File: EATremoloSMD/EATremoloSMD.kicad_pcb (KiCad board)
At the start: 2 copper layers, 31 x 85.1 mm, 38 parts, among them J1 JACK__MONO_2P_NC, J2 BARREL_JACK, J3 JACK__MONO_2P_NC, Q1 Q_NJFET_DSG, Q2 Q_NPN_EBC, Q3 Q_NPN_EBC, Q4 Q_NJFET_DSG, SW1 SW_3PDT_on_on

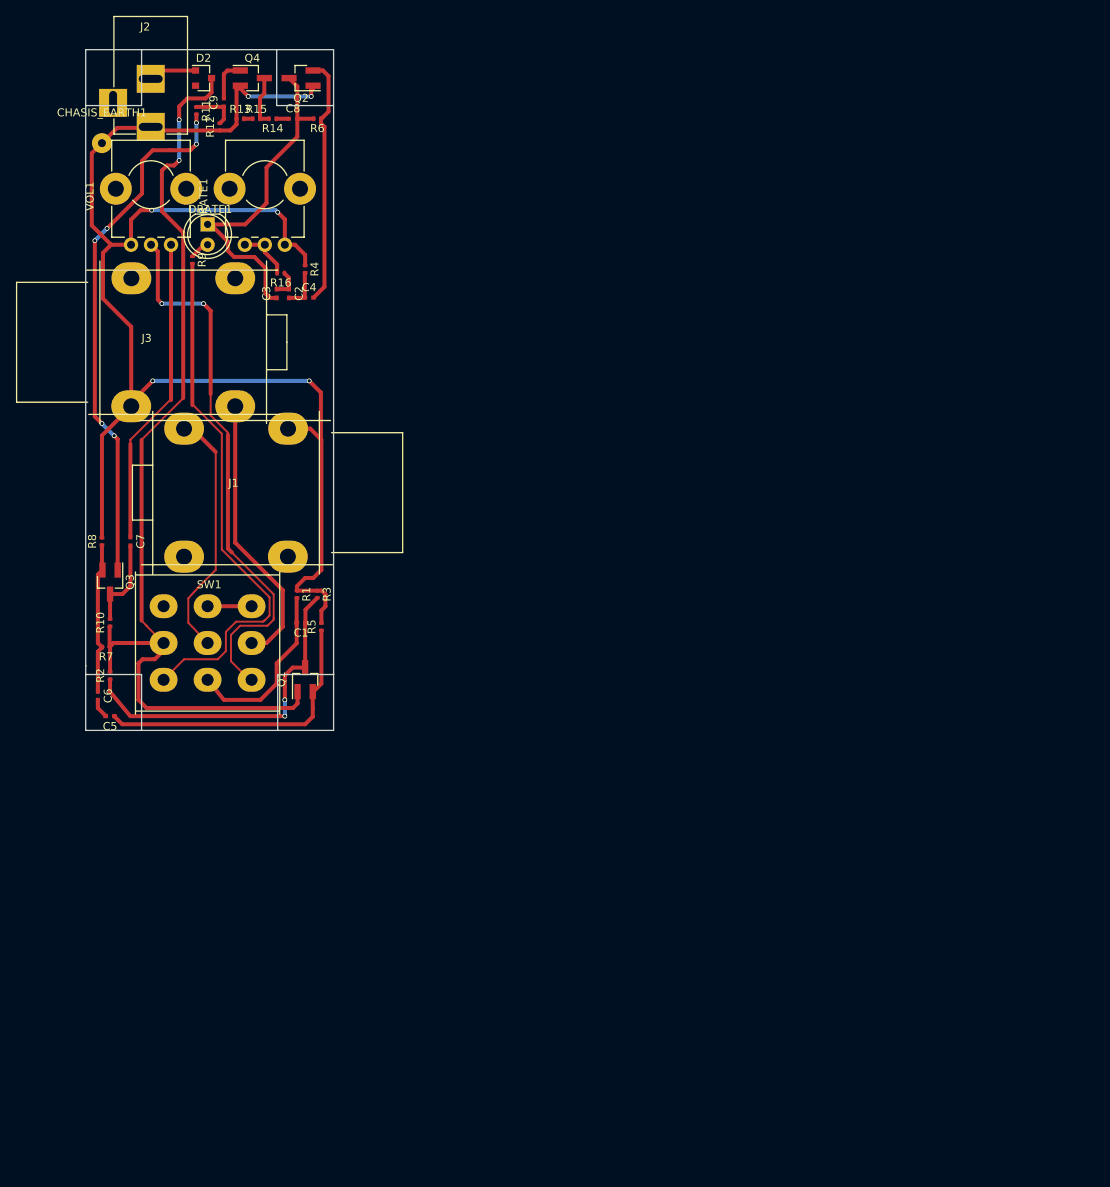
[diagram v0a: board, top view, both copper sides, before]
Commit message: Updated EATremoloSMD
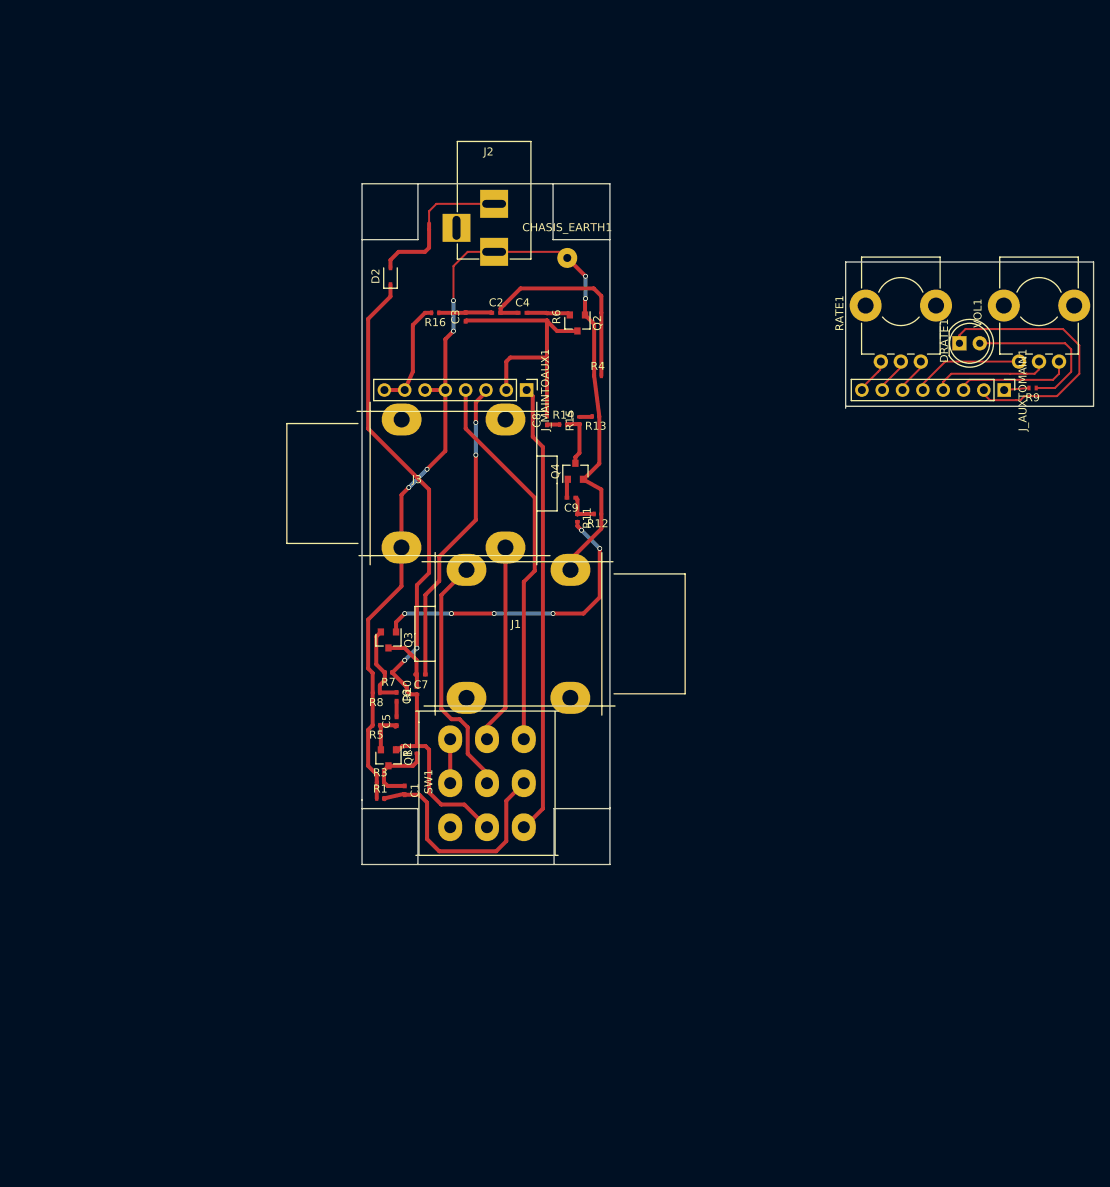
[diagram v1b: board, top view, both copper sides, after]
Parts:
- added J_AUXTOMAIN1: CONN_01X08, Pin_Headers:Pin_Header_Straight_1x08_Pitch2.54mm, F.Cu at (182.1, 86.9)
- added J_MAINTOAUX1: CONN_01X08, Pin_Headers:Pin_Header_Straight_1x08_Pitch2.54mm, F.Cu at (122.4, 86.9)
- D2: footprint Diodes_SMD:D_SOT-23_ANK -> Diodes_SMD:D_SOD-323
- Q1, Q2, Q3, Q4: footprint TO_SOT_Packages_SMD:SOT-23_Handsoldering -> TO_SOT_Packages_SMD:SOT-23
- moved VOL1 112.0 mm to (189.0, 83.3)
- moved R9 106.2 mm to (185.7, 86.6), turned to 180 degrees
- moved DRATE1 95.1 mm to (176.5, 81.0), turned to 0 degrees
- moved RATE1 80.8 mm to (171.7, 83.3)
- moved R11 69.7 mm to (128.8, 102.9)
- moved R12 67.6 mm to (131.3, 102.4), turned to 180 degrees
- moved C9 65.8 mm to (128.0, 100.3), turned to 180 degrees
- moved Q4 63.6 mm to (128.5, 97.0), turned to 90 degrees
- moved CHASIS_EARTH1 59.9 mm to (127.5, 70.4)
- moved R13 58.0 mm to (131.1, 90.2), turned to 180 degrees
- moved R15 55.3 mm to (129.0, 90.7), turned to 90 degrees
- moved R14 52.7 mm to (127.0, 91.2), turned to 0 degrees
- moved C8 49.3 mm to (125.0, 90.7), turned to 90 degrees
- moved Q2 46.2 mm to (128.8, 78.5), turned to 270 degrees
- moved J2 45.7 mm to (118.4, 69.6)
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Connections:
- C3 pad 1: Net-(C3-Pad1) -> /LED_AN
- C7 pad 1: Net-(C7-Pad1) -> /VOL_P3
- C8 pad 2: Net-(C3-Pad1) -> /LED_AN
- DRATE1 pad 1: Net-(C3-Pad1) -> Net-(DRATE1-Pad1)
- Q2 pad 3: Net-(C3-Pad1) -> /LED_AN
- R15 pad 1: Net-(R13-Pad2) -> Net-(Q4-Pad3)
- R15 pad 2: Net-(Q4-Pad3) -> Net-(R13-Pad2)
- R16 pad 2: Net-(R16-Pad2) -> /RATE_P1
- R6 pad 2: Net-(C3-Pad1) -> /LED_AN
- R9 pad 2: Net-(R9-Pad2) -> Net-(J_AUXTOMAIN1-Pad1)
- RATE1 pad 1: /GND -> Net-(J_AUXTOMAIN1-Pad6)
- RATE1 pad 2: Net-(R16-Pad2) -> Net-(J_AUXTOMAIN1-Pad7)
- RATE1 pad 3: Net-(R16-Pad2) -> Net-(J_AUXTOMAIN1-Pad8)
- SW1 pad 3: Net-(R9-Pad2) -> /LED_CA
- SW1 pad 9: Net-(SW1-Pad9) -> /VOL_P2
- VOL1 pad 1: Net-(C7-Pad1) -> Net-(J_AUXTOMAIN1-Pad3)
- VOL1 pad 2: Net-(SW1-Pad9) -> Net-(J_AUXTOMAIN1-Pad4)
- VOL1 pad 3: /GND -> Net-(J_AUXTOMAIN1-Pad5)
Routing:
- net Net-(SW1-Pad9): track 69.4 -> 0.00 mm, vias 2 -> 0
- net Net-(R9-Pad2): track 66.1 -> 0.00 mm
- net /LED_CA: track 0.00 -> 56.5 mm
- net /GND: track 186.7 -> 134.0 mm
- net /VOL_P2: track 0.00 -> 47.8 mm
- net Net-(C3-Pad1): track 43.1 -> 0.00 mm
- net /+9V: track 123.6 -> 84.8 mm
- net Net-(C7-Pad1): track 38.7 -> 0.00 mm
- net /VOL_P3: track 0.00 -> 38.7 mm, vias 0 -> 2
- net /LED_AN: track 0.00 -> 35.4 mm
- net Net-(DRATE1-Pad1): track 0.00 -> 34.8 mm
- net Net-(C1-Pad1): track 42.2 -> 9.93 mm, vias 2 -> 0
- net Net-(C5-Pad1): track 36.9 -> 5.46 mm
- net Net-(Q3-Pad1): track 66.2 -> 38.6 mm
- net Net-(C4-Pad2): track 31.1 -> 5.47 mm
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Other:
- board size 31 x 85.1 mm -> 91.4 x 85.1 mm

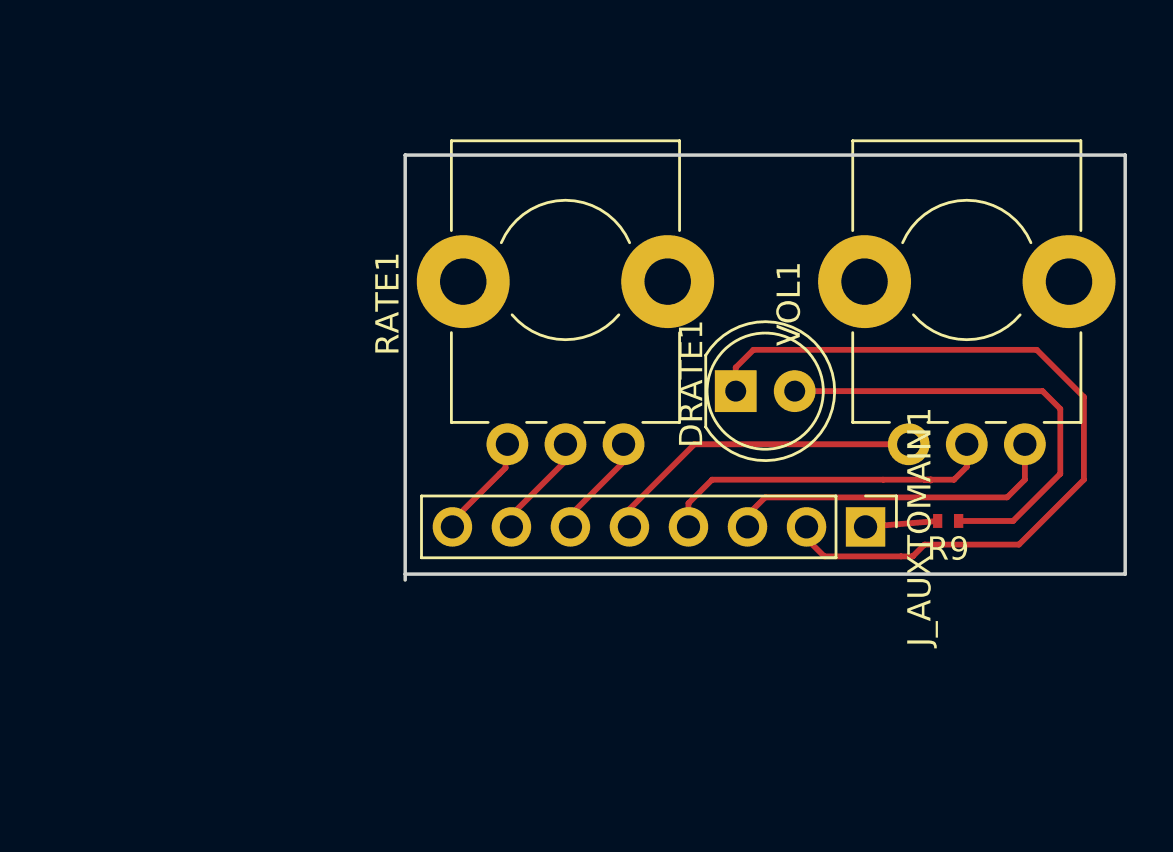
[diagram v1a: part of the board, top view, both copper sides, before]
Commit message: EAMTremoloSMD update
pcb header alignment
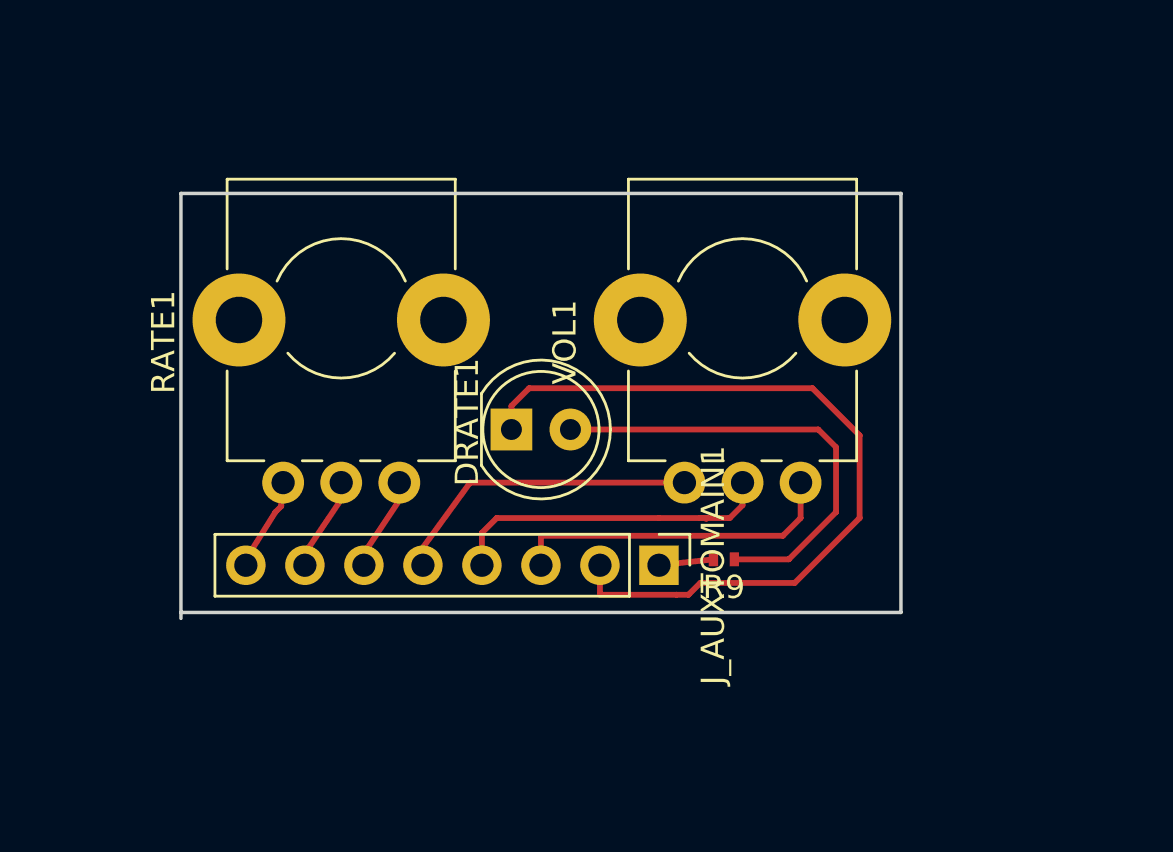
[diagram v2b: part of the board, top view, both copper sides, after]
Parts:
- moved DRATE1 9.79 mm to (166.9, 82.7)
- moved R9 9.79 mm to (176.0, 88.3)
- moved RATE1 9.79 mm to (162.1, 85.0)
- moved VOL1 9.79 mm to (179.3, 85.0)
- moved J_AUXTOMAIN1 9.04 mm to (173.2, 88.5)
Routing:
- net Net-(J_AUXTOMAIN1-Pad1): track 3.12 -> 2.36 mm
- net Net-(J_AUXTOMAIN1-Pad4): track 15.0 -> 14.5 mm
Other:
- board size 91.4 x 85.1 mm -> 81.8 x 85.1 mm

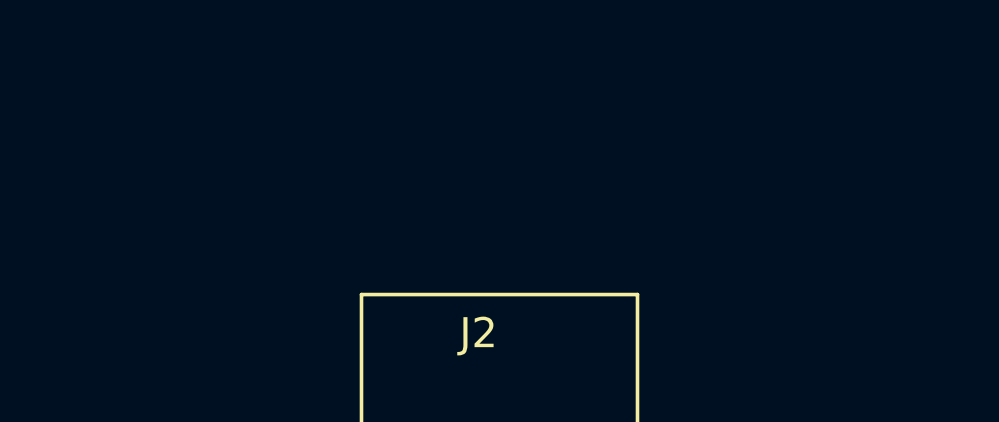
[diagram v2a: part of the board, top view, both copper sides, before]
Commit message: Board Description Updates
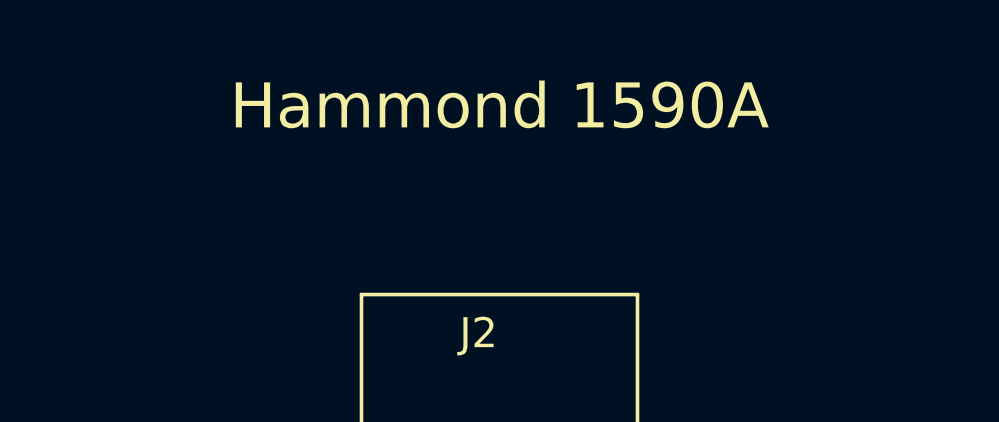
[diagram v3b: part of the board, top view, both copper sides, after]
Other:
- board text added: "Hammond 1590A"
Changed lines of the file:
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@@
     (links 68)
     (no_connects 0)
-    (area 92.180999 55.370999 195.201 146.252001)
+    (area 92.180999 48.33 185.549 146.252001)
     (thickness 1.6)
-    (drawings 18)
+    (drawings 19)
     (tracks 270)
     (zones 0)
@@
       (rotate (xyz 0 0 0))
     )
+  )
+  (gr_text "Hammond 1590A" (at 118.364 49.53) (layer F.SilkS)
+    (effects (font (size 1.5 1.5) (thickness 0.3)))
   )
   (gr_line (start 183.642 90.551) (end 152.654 90.551) (angle 90) (layer Edge.Cuts) (width 0.15))
@@
   (segment (start 123.444 109.474) (end 123.444 100.33) (width 0.5) (layer F.Cu) (net 36))
   (segment (start 122.075 110.843) (end 123.444 109.474) (width 0.5) (layer F.Cu) (net 36))
-  (segment (start 165.608 88.519) (end 165.608 87.122) (width 0.25) (layer F.Cu) (net 37) (status 400000))
+  (segment (start 165.608 88.519) (end 165.608 87.122) (width 0.25) (layer F.Cu) (net 37))
   (segment (start 165.608 87.122) (end 166.243 86.487) (width 0.25) (layer F.Cu) (net 37))
   (segment (start 173.228 86.487) (end 166.243 86.487) (width 0.25) (layer F.Cu) (net 37))

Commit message: updates
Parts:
- SW1: footprint custom_sw:SW_3PDT_W18MM_L17.3MM_P5.3MM_D2MM -> custom_sw:SW_3PDT_W18MM_L17.3MM_P5.3MM_D2MM_SolderLugs
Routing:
- net /LED_CA: track 56.5 -> 57.1 mm

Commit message: BoardUpdate
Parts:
- C1, C2, C3, C4, C5, C6, C7, C8, C9: footprint Capacitors_SMD:C_0402_NoSilk -> Capacitors_SMD:C_0805
- R1, R10, R11, R12, R13, R14, R15, R16, R2, R3, R4, R5, R6, R7, R8, R9: footprint Resistors_SMD:R_0402_NoSilk -> Resistors_SMD:R_0805
- moved J_AUXTOMAIN1 114.1 mm to (108.0, 182.1)
- moved VOL1 113.5 mm to (114.0, 177.8)
- moved RATE1 113.5 mm to (96.8, 177.8)
- moved DRATE1 113.4 mm to (101.7, 175.5)
- moved R9 109.9 mm to (109.4, 175.6), turned to 0 degrees
- moved C8 26.5 mm to (98.5, 90.6), turned to 180 degrees
- moved R14 24.5 mm to (102.5, 90.4), turned to 270 degrees
- moved R13 23.6 mm to (107.4, 90.4), turned to 270 degrees
- moved R16 23.2 mm to (90.6, 88.2), turned to 270 degrees
- moved R6 20.1 mm to (106.9, 86.7)
- moved C2 20.1 mm to (99.3, 82.5)
- moved Q1 20.0 mm to (89.9, 145.9)
- moved Q2 19.7 mm to (110.9, 86.6)
- moved C4 19.5 mm to (103.5, 83.5), turned to 270 degrees
- moved R2 19.1 mm to (92.7, 142.2)
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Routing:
- net /GND: track 134.0 -> 171.1 mm, vias 6 -> 4
- net Net-(C1-Pad1): track 9.93 -> 44.2 mm
- net Net-(C6-Pad1): track 10.7 -> 38.3 mm
- net /VOL_P3: track 38.7 -> 17.0 mm
- net Net-(C1-Pad2): track 29.8 -> 10.6 mm
- net Net-(J_AUXTOMAIN1-Pad1): track 2.36 -> 18.7 mm
- net Net-(Q3-Pad1): track 38.6 -> 22.8 mm, vias 6 -> 2
- net Net-(DRATE1-Pad2): track 19.8 -> 4.34 mm
- net Net-(DRATE1-Pad1): track 34.5 -> 49.4 mm
- net Net-(C7-Pad2): track 7.75 -> 19.2 mm
- net Net-(C5-Pad1): track 5.46 -> 12.0 mm
- net /LED_AN: track 35.4 -> 29.0 mm
- net /VOL_P2: track 47.8 -> 54.0 mm
- net /+9V: track 84.8 -> 91.0 mm
- net Net-(Q4-Pad3): track 6.72 -> 12.8 mm
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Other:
- board size 81.8 x 85.1 mm -> 31.1 x 114.2 mm
- board text removed: "Hammond 1590A"

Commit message: Update
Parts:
- removed J_AUXTOMAIN1, J_MAINTOAUX1: CONN_01X08, Pin_Headers:Pin_Header_Straight_1x08_Pitch2.54mm
- added J_AUX2MAIN_1: CONN_01X04, Pin_Headers:Pin_Header_Straight_1x04_Pitch2.54mm, F.Cu at (125.7, 93.2)
- added J_AUX2MAIN_2: CONN_01X04, Pin_Headers:Pin_Header_Straight_1x04_Pitch2.54mm, F.Cu at (153.7, 93.2)
- added J_MAIN2AUX_1: CONN_01X04, Pin_Headers:Pin_Header_Straight_1x04_Pitch2.54mm, F.Cu at (89.2, 93.7)
- added J_MAIN2AUX_2: CONN_01X04, Pin_Headers:Pin_Header_Straight_1x04_Pitch2.54mm, F.Cu at (116.6, 93.3)
- C1, C2, C3, C4, C5, C6, C7, C8, C9, D2, Q1, Q2, Q3, Q4, R1, R10, R11, R12, R13, R14, R15, R2, R3, R4, R5, R6, R7, R8, R9: moved to B.Cu
- R16: value 1K -> 4K7; moved to B.Cu
- moved R9 98.3 mm to (145.4, 84.2), turned to 90 degrees
- moved RATE1 92.7 mm to (136.1, 93.9)
- moved VOL1 90.7 mm to (148.2, 93.9)
- moved DRATE1 90.3 mm to (139.7, 93.6), turned to 90 degrees
- moved R5 29.3 mm to (117.2, 141.1)
- moved R3 26.1 mm to (90.2, 140.1), turned to 270 degrees
- moved Q1 25.8 mm to (115.7, 145.5)
- moved C5 24.9 mm to (114.0, 130.3), turned to 180 degrees
- moved R11 23.8 mm to (89.8, 105.0)
- moved C1 22.9 mm to (90.2, 144.0), turned to 270 degrees
- moved Q4 21.0 mm to (94.5, 89.5), turned to 0 degrees
- moved R12 20.3 mm to (96.3, 107.1), turned to 90 degrees
- moved C9 16.1 mm to (96.3, 102.7)
- moved R13 13.7 mm to (94.5, 86.1), turned to 0 degrees
- moved R1 12.2 mm to (115.4, 126.9)
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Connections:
- C3 pad 1: /LED_AN -> /LED_CA
- C8 pad 2: /LED_AN -> /LED_CA
- Q2 pad 1: /GND -> Net-(C4-Pad2)
- Q2 pad 2: Net-(C4-Pad2) -> /GND
- Q2 pad 3: /LED_AN -> /LED_CA
- Q3 pad 1: Net-(Q3-Pad1) -> Net-(C6-Pad1)
- Q3 pad 2: Net-(C6-Pad1) -> Net-(Q3-Pad2)
- R11 pad 2: Net-(Q3-Pad1) -> Net-(Q3-Pad2)
- R6 pad 2: /LED_AN -> /LED_CA
- SW1 pad 3: /LED_CA -> /LED_AN
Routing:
- net Net-(C1-Pad2): track 10.6 -> 66.9 mm
- net /LED_AN: track 29.0 -> 78.4 mm, vias 0 -> 2
- net /LED_CA: track 62.7 -> 32.1 mm, vias 0 -> 4
- net Net-(DRATE1-Pad1): track 49.4 -> 20.4 mm
- net /+9V: track 91.0 -> 118.3 mm, vias 2 -> 4
- net Net-(Q3-Pad1): track 22.8 -> 0.00 mm, vias 2 -> 0
- net Net-(C5-Pad2): track 4.20 -> 23.2 mm, vias 0 -> 2
- net Net-(C7-Pad2): track 19.2 -> 35.6 mm, vias 0 -> 2
- net Net-(C2-Pad2): track 25.0 -> 13.0 mm, vias 0 -> 2
- net Net-(J_AUX2MAIN_2-Pad4): track 18.7 -> 9.48 mm
- net Net-(D2-Pad2): track 19.9 -> 10.9 mm
- net Net-(J_AUX2MAIN_1-Pad3): track 6.25 -> 13.9 mm
- net Net-(C9-Pad2): track 5.84 -> 12.4 mm
- net Net-(C5-Pad1): track 12.0 -> 18.3 mm
- net Net-(Q3-Pad2): track 0.00 -> 5.24 mm
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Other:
- board size 31.1 x 114.2 mm -> 67.8 x 85.1 mm

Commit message: update
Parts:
- moved J_AUX2MAIN_2 7.99 mm to (149.7, 86.3)
- moved DRATE1 7.87 mm to (136.0, 86.6)
- moved R9 7.87 mm to (141.7, 77.2)
- moved RATE1 7.87 mm to (132.5, 86.9)
- moved VOL1 7.87 mm to (144.5, 86.9)
- moved J_AUX2MAIN_1 7.75 mm to (122.3, 86.3)
- moved R15 0.71 mm to (100.5, 89.4)
- moved J_MAIN2AUX_1 0.38 mm to (89.2, 93.3)
- moved SW1 0.13 mm to (102.9, 145.2)
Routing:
- net /RATE_P1: track 14.4 -> 10.2 mm
- net Net-(Q4-Pad3): track 10.9 -> 12.3 mm
- net /LED_CA: track 32.1 -> 30.6 mm
- net Net-(J_AUX2MAIN_2-Pad1): track 13.8 -> 15.1 mm
- net /GND: track 173.7 -> 172.6 mm
- net Net-(Q3-Pad2): track 5.24 -> 6.36 mm
- net Net-(C6-Pad1): track 34.7 -> 35.6 mm
- net Net-(D2-Pad2): track 10.9 -> 10.1 mm
- net Net-(C7-Pad2): track 35.6 -> 36.3 mm
- net Net-(C5-Pad1): track 18.3 -> 18.8 mm
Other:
- board size 67.8 x 85.1 mm -> 64.1 x 85.1 mm
- rule via_min_size: 0.4 -> 0.399999

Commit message: Updates
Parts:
- C1, C2, C3, C4, C5, C6, C7, C8, C9: footprint Capacitors_SMD:C_0805 -> Capacitors_SMD:C_0805_HandSoldering
- R1, R10, R11, R12, R13, R14, R15, R16, R2, R3, R4, R5, R6, R7, R8, R9: footprint Resistors_SMD:R_0805 -> Capacitors_SMD:C_0805_HandSoldering
- moved DRATE1 88.8 mm to (102.9, 169.1)
- moved J_AUX2MAIN_1 88.8 mm to (89.2, 168.7)
- moved J_AUX2MAIN_2 88.8 mm to (116.6, 168.7)
- moved R9 88.8 mm to (108.6, 159.7)
- moved RATE1 88.8 mm to (99.3, 169.3)
- moved VOL1 88.8 mm to (111.4, 169.3)
- moved C4 2.35 mm to (105.3, 86.3)
- moved R8 2.03 mm to (90.2, 134.0)
- moved C2 1.59 mm to (104.6, 90.9)
- moved C3 1.54 mm to (100.5, 83.9)
- moved R1 1.40 mm to (114.0, 127.0)
- moved Q2 1.08 mm to (109.4, 84.5)
- moved R3 1.08 mm to (90.1, 139.0)
- moved R6 1.08 mm to (109.4, 87.6)
- moved R12 0.99 mm to (96.0, 108.0)
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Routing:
- net Net-(C6-Pad1): track 35.6 -> 29.9 mm
- net /GND: track 172.6 -> 174.9 mm
- net Net-(C4-Pad2): track 4.60 -> 6.87 mm
- net Net-(C5-Pad2): track 23.2 -> 21.0 mm
- net Net-(C2-Pad1): track 15.7 -> 17.3 mm
- net /LED_CA: track 30.6 -> 32.2 mm
- net Net-(C2-Pad2): track 13.1 -> 14.2 mm
- net Net-(C1-Pad1): track 48.7 -> 49.8 mm
- net Net-(C5-Pad1): track 18.8 -> 17.8 mm
- net Net-(C1-Pad2): track 67.0 -> 68.0 mm
- net Net-(Q4-Pad3): track 12.3 -> 11.4 mm
- net Net-(C9-Pad1): track 8.98 -> 9.71 mm
- net Net-(C9-Pad2): track 12.4 -> 11.7 mm
- net /+9V: track 118.7 -> 118.1 mm
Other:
- board size 64.1 x 85.1 mm -> 31 x 102.3 mm
